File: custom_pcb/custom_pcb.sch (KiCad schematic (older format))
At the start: 205 parts, among them J1 USB_mini_micro_B, K0 KEYSW, K1 KEYSW, K10 KEYSW, K11 KEYSW, K12 KEYSW, K13 KEYSW, K14 KEYSW, K15 KEYSW, K16 KEYSW, K17 KEYSW, K18 KEYSW, K19 KEYSW, K2 KEYSW, K20 KEYSW, K21 KEYSW, K22 KEYSW, K23 KEYSW, K24 KEYSW, K25 KEYSW, K26 KEYSW, K27 KEYSW, K28 KEYSW, K29 KEYSW, K3 KEYSW, K30 KEYSW, K31 KEYSW, K32 KEYSW, K33 KEYSW, K34 KEYSW, K35 KEYSW, K36 KEYSW, K37 KEYSW, K38 KEYSW, K39 KEYSW, K4 KEYSW, K40 KEYSW, K41 KEYSW, K42 KEYSW, K43 KEYSW, K44 KEYSW, K45 KEYSW, K46 KEYSW, K47 KEYSW, K48 KEYSW, K49 KEYSW, K5 KEYSW, K50 KEYSW, K51 KEYSW, K52 KEYSW, K53 KEYSW, K54 KEYSW, K55 KEYSW, K56 KEYSW, K57 KEYSW, K58 KEYSW, K59 KEYSW, K6 KEYSW, K60 KEYSW, K61 KEYSW, K62 KEYSW, K63 KEYSW, K64 KEYSW, K65 KEYSW, K66 KEYSW, K67 KEYSW, K68 KEYSW, K69 KEYSW, K7 KEYSW, K70 KEYSW, K71 KEYSW, K72 KEYSW, K73 KEYSW, K74 KEYSW, K75 KEYSW, K76 KEYSW, K77 KEYSW, K78 KEYSW, K79 KEYSW, K8 KEYSW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

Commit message: cpcb more routing
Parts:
- removed D89, D90, D91, D92, D93, D94, D95, D96, D97, D98, D99: D, Diodes_SMD:D_SOD-123, symbol D
- removed K92, K93, K94, K95, K96, K97, K98, K99: KEYSW, cherry_rgb:CHERRY_PLATE_NH_100H, symbol KEYSW
- renumbered K90 to MOUSE0, K91 to MOUSE1, K89 to MOUSE2
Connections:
- net labels removed: col9
- wire segments 112 -> 108
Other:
- moved on the sheet: MOUSE0, MOUSE1, MOUSE2

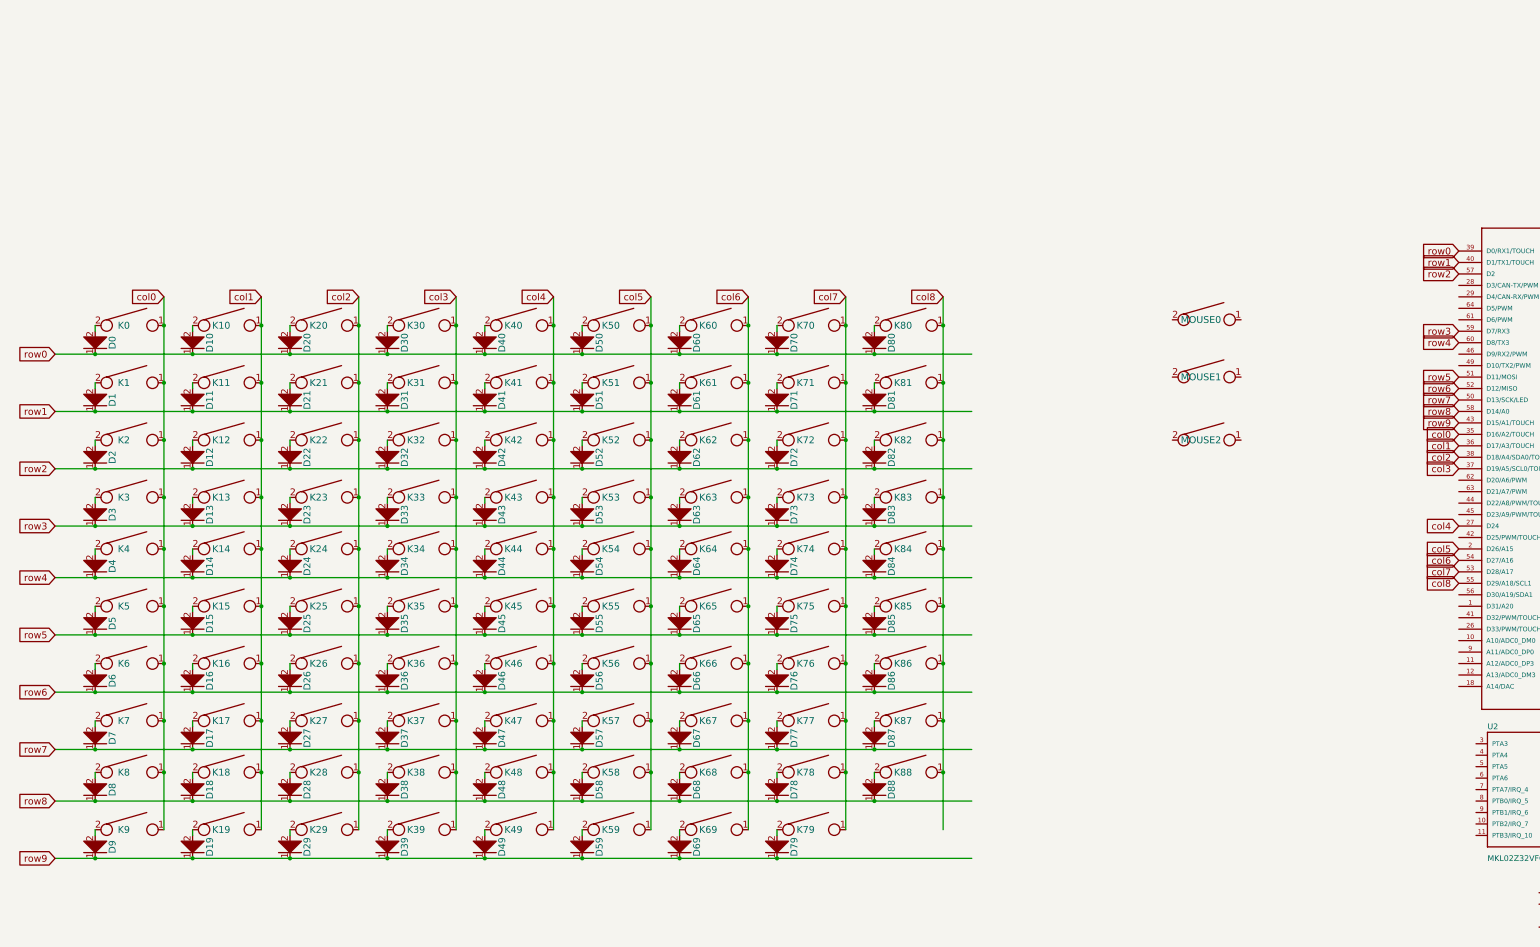
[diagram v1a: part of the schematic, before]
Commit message: cpcb switched to 7x14 matrix finished first pass routing
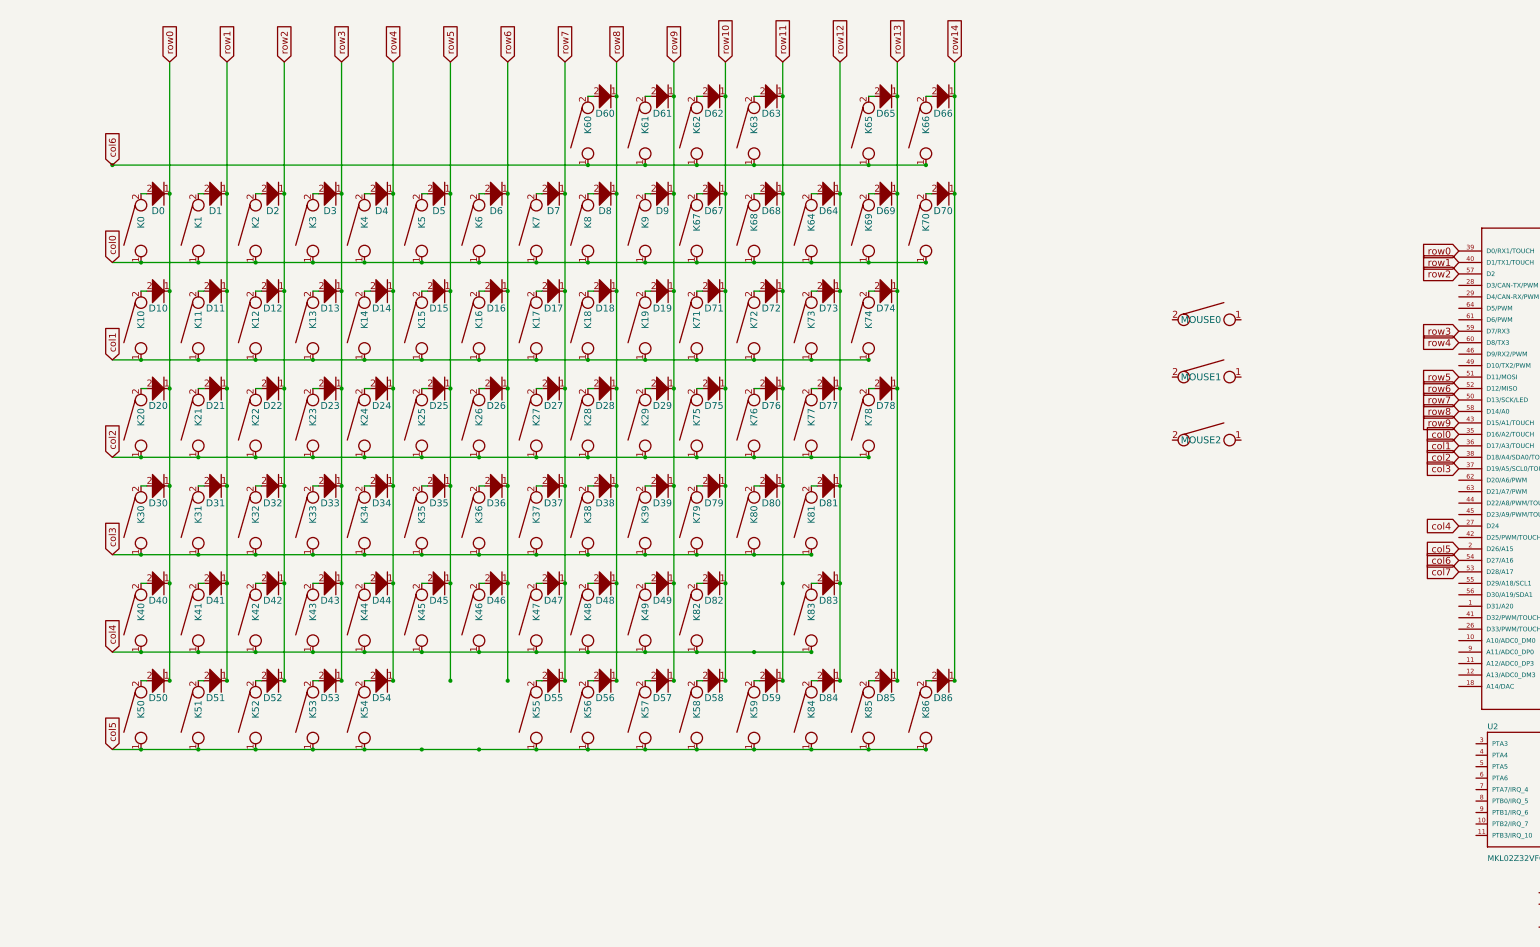
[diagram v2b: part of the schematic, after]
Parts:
- removed D87, D88: D, Diodes_SMD:D_SOD-123, symbol D
- removed K87, K88: KEYSW, cherry_rgb:CHERRY_PLATE_NH_100H, symbol KEYSW
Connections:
- net labels added: row10, row11, row12, row13, row14
- net labels removed: col8
- wire segments 108 -> 109
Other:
- moved on the sheet: D0, D1, D10, D11, D12, D13, D14, D15, D16, D17, D18, D19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

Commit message: cpcb routing of rows and columns complete
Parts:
- added P1: CONN_01X08, Connectors_Molex:Molex_PicoBlade_53261-0871_08x1.25mm_Angled, symbol CONN_01X08
- added U4, U5, U6: STP16CP05, Housings_SSOP:TSSOP-24_4.4x7.8mm_Pitch0.65mm, symbol STP16CP05
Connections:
- net col0: now also U1.59 (D7/RX3); no longer U1.35 (D16/A2/TOUCH)
- net col1: now also U1.60 (D8/TX3); no longer U1.36 (D17/A3/TOUCH)
- net col2: now also U1.61 (D6/PWM); no longer U1.38 (D18/A4/SDA0/TOUCH)
- net col3: now also U1.62 (D20/A6/PWM); no longer U1.37 (D19/A5/SCL0/TOUCH)
- net col4: now also U1.63 (D21/A7/PWM); no longer U1.27 (D24)
- net col5: now also U1.64 (D5/PWM); no longer U1.2 (D26/A15)
- net col6: now also U1.35 (D16/A2/TOUCH); no longer U1.54 (D27/A16)
- net row0: now also U1.58 (D14/A0); no longer U1.39 (D0/RX1/TOUCH)
- net row1: now also U1.57 (D2); no longer U1.40 (D1/TX1/TOUCH)
- net row10: now also U1.40 (D1/TX1/TOUCH)
- net row11: now also U1.39 (D0/RX1/TOUCH)
- net row12: now also U1.38 (D18/A4/SDA0/TOUCH)
- net row13: now also U1.37 (D19/A5/SCL0/TOUCH)
- net row14: now also U1.36 (D17/A3/TOUCH)
- net row2: now also U1.56 (D30/A19/SDA1); no longer U1.57 (D2)
- net row3: now also U1.55 (D29/A18/SCL1); no longer U1.59 (D7/RX3)
- net row4: now also U1.46 (D9/RX2/PWM); no longer U1.60 (D8/TX3)
- net row5: now also U1.45 (D23/A9/PWM/TOUCH); no longer U1.51 (D11/MOSI)
- net row6: now also U1.44 (D22/A8/PWM/TOUCH); no longer U1.52 (D12/MISO)
- net row7: now also U1.43 (D15/A1/TOUCH); no longer U1.50 (D13/SCK/LED)
- net row8: now also U1.42 (D25/PWM/TOUCH); no longer U1.58 (D14/A0)
- net row9: now also U1.41 (D32/PWM/TOUCH); no longer U1.43 (D15/A1/TOUCH)
- net TP_DATA: now reaches U1.1 (D31/A20)
- net TP_DATA: now also P1.2 (P2)
- net GND: now reaches U1.15 (VREF-L)
- net GND: now also P1.1 (P1)
- net LED_DATA1: now reaches U1.28 (D3/CAN-TX/PWM)
- net LED_DATA2: now reaches U1.29 (D4/CAN-RX/PWM)
- net LED_CLK: now reaches U1.49 (D10/TX2/PWM)
- net BTN0: now reaches MOUSE0.1
- net BTN0: now also P1.6 (P6)
- net BTN1: now reaches MOUSE1.1
- net BTN1: now also P1.7 (P7)
- net BTN2: now reaches MOUSE2.1
- net BTN2: now also P1.8 (P8)
- net col7: no longer names the net of U1.53 (D28/A17)
- new net LED_DATA0: U1.27 (D24)
- new net TP_5V: P1.5 (P5)
- new net TP_CLK: P1.3 (P3), U1.2 (D26/A15)
- new net TP_RST: P1.4 (P4)
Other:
- note added: "Note that when wiring the LVC9 -> mainboard \nconnector the BTN0 and BTN2 leads need to be\nswapped since the order is reversed here to simplify routing."
- moved on the sheet: D0, D1, D10, D11, D12, D13, D14, D15, D16, D17, D18, D19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

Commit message: wiring cleanup
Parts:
- removed X1: XTAL, symbol XTAL
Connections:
- net GND: now also MOUSE0.2, MOUSE1.2, MOUSE2.2
- net LED_CLK: now also U4.3 (CLK), U5.3 (CLK), U6.3 (CLK)
- net LED_DATA0: now also U4.2 (SDI)
- net LED_DATA1: now also U5.2 (SDI)
- net LED_DATA2: now also U6.2 (SDI)
- net row0: no longer D0.1, D10.1, D20.1, D30.1, D40.1, D50.1
- net row1: no longer D1.1, D11.1, D21.1, D31.1, D41.1, D51.1
- net row10: no longer D58.1, D62.1, D67.1, D71.1, D75.1, D79.1, D82.1
- net row11: no longer D59.1, D63.1, D68.1, D72.1, D76.1, D80.1
- net row12: no longer D64.1, D73.1, D77.1, D81.1, D83.1, D84.1
- net row13: no longer D65.1, D69.1, D74.1, D78.1, D85.1
- net row14: no longer D66.1, D70.1, D86.1
- net row2: no longer D12.1, D2.1, D22.1, D32.1, D42.1, D52.1
- net row3: no longer D13.1, D23.1, D3.1, D33.1, D43.1, D53.1
- net row4: no longer D14.1, D24.1, D34.1, D4.1, D44.1, D54.1
- net row5: no longer D15.1, D25.1, D35.1, D45.1, D5.1
- net row6: no longer D16.1, D26.1, D36.1, D46.1, D6.1
- net row7: no longer D17.1, D27.1, D37.1, D47.1, D55.1, D7.1
- net row8: no longer D18.1, D28.1, D38.1, D48.1, D56.1, D60.1, D8.1
- net row9: no longer D19.1, D29.1, D39.1, D49.1, D57.1, D61.1, D9.1
- new net c0: D0.1, D10.1, D20.1, D30.1, D40.1, D50.1
- new net c1: D1.1, D11.1, D21.1, D31.1, D41.1, D51.1
- new net c10: D58.1, D62.1, D67.1, D71.1, D75.1, D79.1, D82.1
- new net c11: D59.1, D63.1, D68.1, D72.1, D76.1, D80.1
- new net c12: D64.1, D73.1, D77.1, D81.1, D83.1, D84.1
- new net c13: D65.1, D69.1, D74.1, D78.1, D85.1
- new net c14: D66.1, D70.1, D86.1
- new net c2: D12.1, D2.1, D22.1, D32.1, D42.1, D52.1
- new net c3: D13.1, D23.1, D3.1, D33.1, D43.1, D53.1
- new net c4: D14.1, D24.1, D34.1, D4.1, D44.1, D54.1
- new net c5: D15.1, D25.1, D35.1, D45.1, D5.1
- new net c6: D16.1, D26.1, D36.1, D46.1, D6.1
- new net c7: D17.1, D27.1, D37.1, D47.1, D55.1, D7.1
- new net c8: D18.1, D28.1, D38.1, D48.1, D56.1, D60.1, D8.1
- new net c9: D19.1, D29.1, D39.1, D49.1, D57.1, D61.1, D9.1

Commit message: cpcb started led work
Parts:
- added R0, R1, R2, R3, R4, R5, R6: R, symbol R
- added SMD_LED0, SMD_LED1, SMD_LED10, SMD_LED100, SMD_LED101, SMD_LED102, SMD_LED103, SMD_LED104, SMD_LED11, SMD_LED12, SMD_LED13, SMD_LED14, SMD_LED15, SMD_LED16, SMD_LED17, SMD_LED18, SMD_LED19, SMD_LED2, SMD_LED20, SMD_LED21, SMD_LED22, SMD_LED23, SMD_LED24, SMD_LED25, SMD_LED26, SMD_LED27, SMD_LED28, SMD_LED29, SMD_LED3, SMD_LED30, SMD_LED31, SMD_LED32, SMD_LED33, SMD_LED34, SMD_LED35, SMD_LED36, SMD_LED37, SMD_LED38, SMD_LED39, SMD_LED4, SMD_LED40, SMD_LED41, SMD_LED42, SMD_LED43, SMD_LED44, SMD_LED45, SMD_LED46, SMD_LED47, SMD_LED48, SMD_LED49, SMD_LED5, SMD_LED50, SMD_LED51, SMD_LED52, SMD_LED53, SMD_LED54, SMD_LED55, SMD_LED56, SMD_LED57, SMD_LED58, SMD_LED59, SMD_LED6, SMD_LED60, SMD_LED61, SMD_LED62, SMD_LED63, SMD_LED64, SMD_LED65, SMD_LED66, SMD_LED67, SMD_LED68, SMD_LED69, SMD_LED7, SMD_LED70, SMD_LED71, SMD_LED72, SMD_LED73, SMD_LED74, SMD_LED75, SMD_LED76, SMD_LED77, SMD_LED78, SMD_LED79, SMD_LED8, SMD_LED80, SMD_LED81, SMD_LED82, SMD_LED83, SMD_LED84, SMD_LED85, SMD_LED86, SMD_LED87, SMD_LED88, SMD_LED89, SMD_LED9, SMD_LED90, SMD_LED91, SMD_LED92, SMD_LED93, SMD_LED94, SMD_LED95, SMD_LED96, SMD_LED97, SMD_LED98, SMD_LED99: SMLVN6RGB, symbol SMLVN6RGB
- K0, K64: footprint cherry_rgb:CHERRY_PLATE_NH_100H -> cherry_rgb:CHERRY_PLATE_150V
- K20, K56, K78: footprint cherry_rgb:CHERRY_PLATE_NH_100H -> cherry_rgb:CHERRY_PLATE_150H
- K30, MOUSE0, MOUSE2: footprint cherry_rgb:CHERRY_PLATE_NH_100H -> cherry_rgb:CHERRY_PLATE_175H
- K40, K81: footprint cherry_rgb:CHERRY_PLATE_NH_100H -> cherry_rgb:CHERRY_PLATE_225H
- K51, K55: footprint cherry_rgb:CHERRY_PLATE_NH_100H -> cherry_rgb:CHERRY_PLATE_125H
- K54: footprint cherry_rgb:CHERRY_PLATE_NH_100H -> cherry_rgb:CHERRY_PLATE_NH_5000H
- K74: footprint cherry_rgb:CHERRY_PLATE_NH_100H -> cherry_rgb:CHERRY_PLATE_200H
- K83: footprint cherry_rgb:CHERRY_PLATE_NH_100H -> cherry_rgb:CHERRY_PLATE_275H
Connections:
- net row0 is gone; now on net c0: U1.58 (D14/A0)
- net row1 is gone; now on net c1: U1.57 (D2)
- net row10 is gone; now on net c10: U1.40 (D1/TX1/TOUCH)
- net row11 is gone; now on net c11: U1.39 (D0/RX1/TOUCH)
- net row12 is gone; now on net c12: U1.38 (D18/A4/SDA0/TOUCH)
- net row13 is gone; now on net c13: U1.37 (D19/A5/SCL0/TOUCH)
- net row14 is gone; now on net c14: U1.36 (D17/A3/TOUCH)
- net row2 is gone; now on net c2: U1.56 (D30/A19/SDA1)
- net row3 is gone; now on net c3: U1.55 (D29/A18/SCL1)
- net row4 is gone; now on net c4: U1.46 (D9/RX2/PWM)
- net row5 is gone; now on net c5: U1.45 (D23/A9/PWM/TOUCH)
- net row6 is gone; now on net c6: U1.44 (D22/A8/PWM/TOUCH)
- net row7 is gone; now on net c7: U1.43 (D15/A1/TOUCH)
- net row8 is gone; now on net c8: U1.42 (D25/PWM/TOUCH)
- net row9 is gone; now on net c9: U1.41 (D32/PWM/TOUCH)
- net anode5: now reaches U4.10 (OUT5)
- net anode5: now also SMD_LED20.1 (RK), SMD_LED20.2 (GK), SMD_LED20.3 (BK), SMD_LED35.1 (RK), SMD_LED35.2 (GK), SMD_LED35.3 (BK), SMD_LED5.1 (RK), SMD_LED5.2 (GK), SMD_LED5.3 (BK), SMD_LED50.1 (RK), SMD_LED50.2 (GK), SMD_LED50.3 (BK), SMD_LED65.1 (RK), SMD_LED65.2 (GK), SMD_LED65.3 (BK), SMD_LED80.1 (RK), SMD_LED80.2 (GK), SMD_LED80.3 (BK), SMD_LED95.1 (RK), SMD_LED95.2 (GK), SMD_LED95.3 (BK)
- net anode6: now reaches U4.11 (OUT6)
- net anode6: now also SMD_LED21.1 (RK), SMD_LED21.2 (GK), SMD_LED21.3 (BK), SMD_LED36.1 (RK), SMD_LED36.2 (GK), SMD_LED36.3 (BK), SMD_LED51.1 (RK), SMD_LED51.2 (GK), SMD_LED51.3 (BK), SMD_LED6.1 (RK), SMD_LED6.2 (GK), SMD_LED6.3 (BK), SMD_LED66.1 (RK), SMD_LED66.2 (GK), SMD_LED66.3 (BK), SMD_LED81.1 (RK), SMD_LED81.2 (GK), SMD_LED81.3 (BK), SMD_LED96.1 (RK), SMD_LED96.2 (GK), SMD_LED96.3 (BK)
- net anode7: now reaches U4.12 (OUT7)
- net anode7: now also SMD_LED22.1 (RK), SMD_LED22.2 (GK), SMD_LED22.3 (BK), SMD_LED37.1 (RK), SMD_LED37.2 (GK), SMD_LED37.3 (BK), SMD_LED52.1 (RK), SMD_LED52.2 (GK), SMD_LED52.3 (BK), SMD_LED67.1 (RK), SMD_LED67.2 (GK), SMD_LED67.3 (BK), SMD_LED7.1 (RK), SMD_LED7.2 (GK), SMD_LED7.3 (BK), SMD_LED82.1 (RK), SMD_LED82.2 (GK), SMD_LED82.3 (BK), SMD_LED97.1 (RK), SMD_LED97.2 (GK), SMD_LED97.3 (BK)
- net anode8: now reaches U4.13 (OUT8)
- net anode8: now also SMD_LED23.1 (RK), SMD_LED23.2 (GK), SMD_LED23.3 (BK), SMD_LED38.1 (RK), SMD_LED38.2 (GK), SMD_LED38.3 (BK), SMD_LED53.1 (RK), SMD_LED53.2 (GK), SMD_LED53.3 (BK), SMD_LED68.1 (RK), SMD_LED68.2 (GK), SMD_LED68.3 (BK), SMD_LED8.1 (RK), SMD_LED8.2 (GK), SMD_LED8.3 (BK), SMD_LED83.1 (RK), SMD_LED83.2 (GK), SMD_LED83.3 (BK), SMD_LED98.1 (RK), SMD_LED98.2 (GK), SMD_LED98.3 (BK)
- net anode9: now reaches U4.14 (OUT9)
- net anode9: now also SMD_LED24.1 (RK), SMD_LED24.2 (GK), SMD_LED24.3 (BK), SMD_LED39.1 (RK), SMD_LED39.2 (GK), SMD_LED39.3 (BK), SMD_LED54.1 (RK), SMD_LED54.2 (GK), SMD_LED54.3 (BK), SMD_LED69.1 (RK), SMD_LED69.2 (GK), SMD_LED69.3 (BK), SMD_LED84.1 (RK), SMD_LED84.2 (GK), SMD_LED84.3 (BK), SMD_LED9.1 (RK), SMD_LED9.2 (GK), SMD_LED9.3 (BK), SMD_LED99.1 (RK), SMD_LED99.2 (GK), SMD_LED99.3 (BK)
- net anode10: now reaches U4.15 (OUT10)
- net anode10: now also SMD_LED10.1 (RK), SMD_LED10.2 (GK), SMD_LED10.3 (BK), SMD_LED100.1 (RK), SMD_LED100.2 (GK), SMD_LED100.3 (BK), SMD_LED25.1 (RK), SMD_LED25.2 (GK), SMD_LED25.3 (BK), SMD_LED40.1 (RK), SMD_LED40.2 (GK), SMD_LED40.3 (BK), SMD_LED55.1 (RK), SMD_LED55.2 (GK), SMD_LED55.3 (BK), SMD_LED70.1 (RK), SMD_LED70.2 (GK), SMD_LED70.3 (BK), SMD_LED85.1 (RK), SMD_LED85.2 (GK), SMD_LED85.3 (BK)
- net anode11: now reaches U4.16 (OUT11)
- net anode11: now also SMD_LED101.1 (RK), SMD_LED101.2 (GK), SMD_LED101.3 (BK), SMD_LED11.1 (RK), SMD_LED11.2 (GK), SMD_LED11.3 (BK), SMD_LED26.1 (RK), SMD_LED26.2 (GK), SMD_LED26.3 (BK), SMD_LED41.1 (RK), SMD_LED41.2 (GK), SMD_LED41.3 (BK), SMD_LED56.1 (RK), SMD_LED56.2 (GK), SMD_LED56.3 (BK), SMD_LED71.1 (RK), SMD_LED71.2 (GK), SMD_LED71.3 (BK), SMD_LED86.1 (RK), SMD_LED86.2 (GK), SMD_LED86.3 (BK)
- net anode12: now reaches U4.17 (OUT12)
- net anode12: now also SMD_LED102.1 (RK), SMD_LED102.2 (GK), SMD_LED102.3 (BK), SMD_LED12.1 (RK), SMD_LED12.2 (GK), SMD_LED12.3 (BK), SMD_LED27.1 (RK), SMD_LED27.2 (GK), SMD_LED27.3 (BK), SMD_LED42.1 (RK), SMD_LED42.2 (GK), SMD_LED42.3 (BK), SMD_LED57.1 (RK), SMD_LED57.2 (GK), SMD_LED57.3 (BK), SMD_LED72.1 (RK), SMD_LED72.2 (GK), SMD_LED72.3 (BK), SMD_LED87.1 (RK), SMD_LED87.2 (GK), SMD_LED87.3 (BK)
- net anode13: now reaches U4.18 (OUT13)
- net anode13: now also SMD_LED103.1 (RK), SMD_LED103.2 (GK), SMD_LED103.3 (BK), SMD_LED13.1 (RK), SMD_LED13.2 (GK), SMD_LED13.3 (BK), SMD_LED28.1 (RK), SMD_LED28.2 (GK), SMD_LED28.3 (BK), SMD_LED43.1 (RK), SMD_LED43.2 (GK), SMD_LED43.3 (BK), SMD_LED58.1 (RK), SMD_LED58.2 (GK), SMD_LED58.3 (BK), SMD_LED73.1 (RK), SMD_LED73.2 (GK), SMD_LED73.3 (BK), SMD_LED88.1 (RK), SMD_LED88.2 (GK), SMD_LED88.3 (BK)
- net anode14: now reaches U4.19 (OUT14)
- net anode14: now also SMD_LED104.1 (RK), SMD_LED104.2 (GK), SMD_LED104.3 (BK), SMD_LED14.1 (RK), SMD_LED14.2 (GK), SMD_LED14.3 (BK), SMD_LED29.1 (RK), SMD_LED29.2 (GK), SMD_LED29.3 (BK), SMD_LED44.1 (RK), SMD_LED44.2 (GK), SMD_LED44.3 (BK), SMD_LED59.1 (RK), SMD_LED59.2 (GK), SMD_LED59.3 (BK), SMD_LED74.1 (RK), SMD_LED74.2 (GK), SMD_LED74.3 (BK), SMD_LED89.1 (RK), SMD_LED89.2 (GK), SMD_LED89.3 (BK)
- net anode0: now reaches U4.5 (OUT0)
- net anode0: now also SMD_LED0.1 (RK), SMD_LED0.2 (GK), SMD_LED0.3 (BK), SMD_LED15.1 (RK), SMD_LED15.2 (GK), SMD_LED15.3 (BK), SMD_LED30.1 (RK), SMD_LED30.2 (GK), SMD_LED30.3 (BK), SMD_LED45.1 (RK), SMD_LED45.2 (GK), SMD_LED45.3 (BK), SMD_LED60.1 (RK), SMD_LED60.2 (GK), SMD_LED60.3 (BK), SMD_LED75.1 (RK), SMD_LED75.2 (GK), SMD_LED75.3 (BK), SMD_LED90.1 (RK), SMD_LED90.2 (GK), SMD_LED90.3 (BK)
- net anode1: now reaches U4.6 (OUT1)
- net anode1: now also SMD_LED1.1 (RK), SMD_LED1.2 (GK), SMD_LED1.3 (BK), SMD_LED16.1 (RK), SMD_LED16.2 (GK), SMD_LED16.3 (BK), SMD_LED31.1 (RK), SMD_LED31.2 (GK), SMD_LED31.3 (BK), SMD_LED46.1 (RK), SMD_LED46.2 (GK), SMD_LED46.3 (BK), SMD_LED61.1 (RK), SMD_LED61.2 (GK), SMD_LED61.3 (BK), SMD_LED76.1 (RK), SMD_LED76.2 (GK), SMD_LED76.3 (BK), SMD_LED91.1 (RK), SMD_LED91.2 (GK), SMD_LED91.3 (BK)
- net anode2: now reaches U4.7 (OUT2)
- net anode2: now also SMD_LED17.1 (RK), SMD_LED17.2 (GK), SMD_LED17.3 (BK), SMD_LED2.1 (RK), SMD_LED2.2 (GK), SMD_LED2.3 (BK), SMD_LED32.1 (RK), SMD_LED32.2 (GK), SMD_LED32.3 (BK), SMD_LED47.1 (RK), SMD_LED47.2 (GK), SMD_LED47.3 (BK), SMD_LED62.1 (RK), SMD_LED62.2 (GK), SMD_LED62.3 (BK), SMD_LED77.1 (RK), SMD_LED77.2 (GK), SMD_LED77.3 (BK), SMD_LED92.1 (RK), SMD_LED92.2 (GK), SMD_LED92.3 (BK)
- net anode3: now reaches U4.8 (OUT3)
- net anode3: now also SMD_LED18.1 (RK), SMD_LED18.2 (GK), SMD_LED18.3 (BK), SMD_LED3.1 (RK), SMD_LED3.2 (GK), SMD_LED3.3 (BK), SMD_LED33.1 (RK), SMD_LED33.2 (GK), SMD_LED33.3 (BK), SMD_LED48.1 (RK), SMD_LED48.2 (GK), SMD_LED48.3 (BK), SMD_LED63.1 (RK), SMD_LED63.2 (GK), SMD_LED63.3 (BK), SMD_LED78.1 (RK), SMD_LED78.2 (GK), SMD_LED78.3 (BK), SMD_LED93.1 (RK), SMD_LED93.2 (GK), SMD_LED93.3 (BK)
- net anode4: now reaches U4.9 (OUT4)
- net anode4: now also SMD_LED19.1 (RK), SMD_LED19.2 (GK), SMD_LED19.3 (BK), SMD_LED34.1 (RK), SMD_LED34.2 (GK), SMD_LED34.3 (BK), SMD_LED4.1 (RK), SMD_LED4.2 (GK), SMD_LED4.3 (BK), SMD_LED49.1 (RK), SMD_LED49.2 (GK), SMD_LED49.3 (BK), SMD_LED64.1 (RK), SMD_LED64.2 (GK), SMD_LED64.3 (BK), SMD_LED79.1 (RK), SMD_LED79.2 (GK), SMD_LED79.3 (BK), SMD_LED94.1 (RK), SMD_LED94.2 (GK), SMD_LED94.3 (BK)
- net col0 renamed r0
- net col1 renamed r1
- net col2 renamed r2
- net col3 renamed r3
- net col4 renamed r4
- net col5 renamed r5
- net col6 renamed r6
- new net: R6.1, SMD_LED100.5 (GA), SMD_LED101.5 (GA), SMD_LED102.5 (GA), SMD_LED103.5 (GA), SMD_LED104.5 (GA), SMD_LED90.5 (GA), SMD_LED91.5 (GA), SMD_LED92.5 (GA), SMD_LED93.5 (GA), SMD_LED94.5 (GA), SMD_LED95.5 (GA), SMD_LED96.5 (GA), SMD_LED97.5 (GA), SMD_LED98.5 (GA), SMD_LED99.5 (GA)
- new net: R5.1, SMD_LED75.5 (GA), SMD_LED76.5 (GA), SMD_LED77.5 (GA), SMD_LED78.5 (GA), SMD_LED79.5 (GA), SMD_LED80.5 (GA), SMD_LED81.5 (GA), SMD_LED82.5 (GA), SMD_LED83.5 (GA), SMD_LED84.5 (GA), SMD_LED85.5 (GA), SMD_LED86.5 (GA), SMD_LED87.5 (GA), SMD_LED88.5 (GA), SMD_LED89.5 (GA)
- new net: R4.1, SMD_LED60.5 (GA), SMD_LED61.5 (GA), SMD_LED62.5 (GA), SMD_LED63.5 (GA), SMD_LED64.5 (GA), SMD_LED65.5 (GA), SMD_LED66.5 (GA), SMD_LED67.5 (GA), SMD_LED68.5 (GA), SMD_LED69.5 (GA), SMD_LED70.5 (GA), SMD_LED71.5 (GA), SMD_LED72.5 (GA), SMD_LED73.5 (GA), SMD_LED74.5 (GA)
- new net: R3.1, SMD_LED45.5 (GA), SMD_LED46.5 (GA), SMD_LED47.5 (GA), SMD_LED48.5 (GA), SMD_LED49.5 (GA), SMD_LED50.5 (GA), SMD_LED51.5 (GA), SMD_LED52.5 (GA), SMD_LED53.5 (GA), SMD_LED54.5 (GA), SMD_LED55.5 (GA), SMD_LED56.5 (GA), SMD_LED57.5 (GA), SMD_LED58.5 (GA), SMD_LED59.5 (GA)
- new net: R2.1, SMD_LED30.5 (GA), SMD_LED31.5 (GA), SMD_LED32.5 (GA), SMD_LED33.5 (GA), SMD_LED34.5 (GA), SMD_LED35.5 (GA), SMD_LED36.5 (GA), SMD_LED37.5 (GA), SMD_LED38.5 (GA), SMD_LED39.5 (GA), SMD_LED40.5 (GA), SMD_LED41.5 (GA), SMD_LED42.5 (GA), SMD_LED43.5 (GA), SMD_LED44.5 (GA)
- new net: R1.1, SMD_LED15.5 (GA), SMD_LED16.5 (GA), SMD_LED17.5 (GA), SMD_LED18.5 (GA), SMD_LED19.5 (GA), SMD_LED20.5 (GA), SMD_LED21.5 (GA), SMD_LED22.5 (GA), SMD_LED23.5 (GA), SMD_LED24.5 (GA), SMD_LED25.5 (GA), SMD_LED26.5 (GA), SMD_LED27.5 (GA), SMD_LED28.5 (GA), SMD_LED29.5 (GA)
- new net: R0.1, SMD_LED0.5 (GA), SMD_LED1.5 (GA), SMD_LED10.5 (GA), SMD_LED11.5 (GA), SMD_LED12.5 (GA), SMD_LED13.5 (GA), SMD_LED14.5 (GA), SMD_LED2.5 (GA), SMD_LED3.5 (GA), SMD_LED4.5 (GA), SMD_LED5.5 (GA), SMD_LED6.5 (GA), SMD_LED7.5 (GA), SMD_LED8.5 (GA), SMD_LED9.5 (GA)
- new net blue0: SMD_LED0.6 (RA), SMD_LED1.6 (RA), SMD_LED10.6 (RA), SMD_LED11.6 (RA), SMD_LED12.6 (RA), SMD_LED13.6 (RA), SMD_LED14.6 (RA), SMD_LED2.6 (RA), SMD_LED3.6 (RA), SMD_LED4.6 (RA), SMD_LED5.6 (RA), SMD_LED6.6 (RA), SMD_LED7.6 (RA), SMD_LED8.6 (RA), SMD_LED9.6 (RA)
- new net blue1: SMD_LED15.6 (RA), SMD_LED16.6 (RA), SMD_LED17.6 (RA), SMD_LED18.6 (RA), SMD_LED19.6 (RA), SMD_LED20.6 (RA), SMD_LED21.6 (RA), SMD_LED22.6 (RA), SMD_LED23.6 (RA), SMD_LED24.6 (RA), SMD_LED25.6 (RA), SMD_LED26.6 (RA), SMD_LED27.6 (RA), SMD_LED28.6 (RA), SMD_LED29.6 (RA)
- new net blue2: SMD_LED30.6 (RA), SMD_LED31.6 (RA), SMD_LED32.6 (RA), SMD_LED33.6 (RA), SMD_LED34.6 (RA), SMD_LED35.6 (RA), SMD_LED36.6 (RA), SMD_LED37.6 (RA), SMD_LED38.6 (RA), SMD_LED39.6 (RA), SMD_LED40.6 (RA), SMD_LED41.6 (RA), SMD_LED42.6 (RA), SMD_LED43.6 (RA), SMD_LED44.6 (RA)
- new net blue3: SMD_LED45.6 (RA), SMD_LED46.6 (RA), SMD_LED47.6 (RA), SMD_LED48.6 (RA), SMD_LED49.6 (RA), SMD_LED50.6 (RA), SMD_LED51.6 (RA), SMD_LED52.6 (RA), SMD_LED53.6 (RA), SMD_LED54.6 (RA), SMD_LED55.6 (RA), SMD_LED56.6 (RA), SMD_LED57.6 (RA), SMD_LED58.6 (RA), SMD_LED59.6 (RA)
- new net blue4: SMD_LED60.6 (RA), SMD_LED61.6 (RA), SMD_LED62.6 (RA), SMD_LED63.6 (RA), SMD_LED64.6 (RA), SMD_LED65.6 (RA), SMD_LED66.6 (RA), SMD_LED67.6 (RA), SMD_LED68.6 (RA), SMD_LED69.6 (RA), SMD_LED70.6 (RA), SMD_LED71.6 (RA), SMD_LED72.6 (RA), SMD_LED73.6 (RA), SMD_LED74.6 (RA)
- new net blue5: SMD_LED75.6 (RA), SMD_LED76.6 (RA), SMD_LED77.6 (RA), SMD_LED78.6 (RA), SMD_LED79.6 (RA), SMD_LED80.6 (RA), SMD_LED81.6 (RA), SMD_LED82.6 (RA), SMD_LED83.6 (RA), SMD_LED84.6 (RA), SMD_LED85.6 (RA), SMD_LED86.6 (RA), SMD_LED87.6 (RA), SMD_LED88.6 (RA), SMD_LED89.6 (RA)
- new net blue6: SMD_LED100.6 (RA), SMD_LED101.6 (RA), SMD_LED102.6 (RA), SMD_LED103.6 (RA), SMD_LED104.6 (RA), SMD_LED90.6 (RA), SMD_LED91.6 (RA), SMD_LED92.6 (RA), SMD_LED93.6 (RA), SMD_LED94.6 (RA), SMD_LED95.6 (RA), SMD_LED96.6 (RA), SMD_LED97.6 (RA), SMD_LED98.6 (RA), SMD_LED99.6 (RA)
- new net green0: SMD_LED0.4 (BA), SMD_LED1.4 (BA), SMD_LED10.4 (BA), SMD_LED11.4 (BA), SMD_LED12.4 (BA), SMD_LED13.4 (BA), SMD_LED14.4 (BA), SMD_LED2.4 (BA), SMD_LED3.4 (BA), SMD_LED4.4 (BA), SMD_LED5.4 (BA), SMD_LED6.4 (BA), SMD_LED7.4 (BA), SMD_LED8.4 (BA), SMD_LED9.4 (BA)
- new net green1: SMD_LED15.4 (BA), SMD_LED16.4 (BA), SMD_LED17.4 (BA), SMD_LED18.4 (BA), SMD_LED19.4 (BA), SMD_LED20.4 (BA), SMD_LED21.4 (BA), SMD_LED22.4 (BA), SMD_LED23.4 (BA), SMD_LED24.4 (BA), SMD_LED25.4 (BA), SMD_LED26.4 (BA), SMD_LED27.4 (BA), SMD_LED28.4 (BA), SMD_LED29.4 (BA)
- new net green2: SMD_LED30.4 (BA), SMD_LED31.4 (BA), SMD_LED32.4 (BA), SMD_LED33.4 (BA), SMD_LED34.4 (BA), SMD_LED35.4 (BA), SMD_LED36.4 (BA), SMD_LED37.4 (BA), SMD_LED38.4 (BA), SMD_LED39.4 (BA), SMD_LED40.4 (BA), SMD_LED41.4 (BA), SMD_LED42.4 (BA), SMD_LED43.4 (BA), SMD_LED44.4 (BA)
- new net green3: SMD_LED45.4 (BA), SMD_LED46.4 (BA), SMD_LED47.4 (BA), SMD_LED48.4 (BA), SMD_LED49.4 (BA), SMD_LED50.4 (BA), SMD_LED51.4 (BA), SMD_LED52.4 (BA), SMD_LED53.4 (BA), SMD_LED54.4 (BA), SMD_LED55.4 (BA), SMD_LED56.4 (BA), SMD_LED57.4 (BA), SMD_LED58.4 (BA), SMD_LED59.4 (BA)
- new net green4: SMD_LED60.4 (BA), SMD_LED61.4 (BA), SMD_LED62.4 (BA), SMD_LED63.4 (BA), SMD_LED64.4 (BA), SMD_LED65.4 (BA), SMD_LED66.4 (BA), SMD_LED67.4 (BA), SMD_LED68.4 (BA), SMD_LED69.4 (BA), SMD_LED70.4 (BA), SMD_LED71.4 (BA), SMD_LED72.4 (BA), SMD_LED73.4 (BA), SMD_LED74.4 (BA)
- new net green5: SMD_LED75.4 (BA), SMD_LED76.4 (BA), SMD_LED77.4 (BA), SMD_LED78.4 (BA), SMD_LED79.4 (BA), SMD_LED80.4 (BA), SMD_LED81.4 (BA), SMD_LED82.4 (BA), SMD_LED83.4 (BA), SMD_LED84.4 (BA), SMD_LED85.4 (BA), SMD_LED86.4 (BA), SMD_LED87.4 (BA), SMD_LED88.4 (BA), SMD_LED89.4 (BA)
- new net green6: SMD_LED100.4 (BA), SMD_LED101.4 (BA), SMD_LED102.4 (BA), SMD_LED103.4 (BA), SMD_LED104.4 (BA), SMD_LED90.4 (BA), SMD_LED91.4 (BA), SMD_LED92.4 (BA), SMD_LED93.4 (BA), SMD_LED94.4 (BA), SMD_LED95.4 (BA), SMD_LED96.4 (BA), SMD_LED97.4 (BA), SMD_LED98.4 (BA), SMD_LED99.4 (BA)
- new net red0: R0.2
- new net red1: R1.2
- new net red2: R2.2
- new net red3: R3.2
- new net red4: R4.2
- new net red5: R5.2
- new net red6: R6.2
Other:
- note added: "Wire LEDs using common anode."
- moved on the sheet: D0, D1, D10, D11, D12, D13, D14, D15, D16, D17, D18, D19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

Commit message: cpcb led layout
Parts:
- R0, R1, R2, R3, R4, R5, R6: footprint (none) -> Resistors_SMD:R_0402
- SMD_LED0, SMD_LED1, SMD_LED10, SMD_LED100, SMD_LED101, SMD_LED102, SMD_LED103, SMD_LED104, SMD_LED11, SMD_LED12, SMD_LED13, SMD_LED14, SMD_LED15, SMD_LED16, SMD_LED17, SMD_LED18, SMD_LED19, SMD_LED2, SMD_LED20, SMD_LED21, SMD_LED22, SMD_LED23, SMD_LED24, SMD_LED25, SMD_LED26, SMD_LED27, SMD_LED28, SMD_LED29, SMD_LED3, SMD_LED30, SMD_LED31, SMD_LED32, SMD_LED33, SMD_LED34, SMD_LED35, SMD_LED36, SMD_LED37, SMD_LED38, SMD_LED39, SMD_LED4, SMD_LED40, SMD_LED41, SMD_LED42, SMD_LED43, SMD_LED44, SMD_LED45, SMD_LED46, SMD_LED47, SMD_LED48, SMD_LED49, SMD_LED5, SMD_LED50, SMD_LED51, SMD_LED52, SMD_LED53, SMD_LED54, SMD_LED55, SMD_LED56, SMD_LED57, SMD_LED58, SMD_LED59, SMD_LED6, SMD_LED60, SMD_LED61, SMD_LED62, SMD_LED63, SMD_LED64, SMD_LED65, SMD_LED66, SMD_LED67, SMD_LED68, SMD_LED69, SMD_LED7, SMD_LED70, SMD_LED71, SMD_LED72, SMD_LED73, SMD_LED74, SMD_LED75, SMD_LED76, SMD_LED77, SMD_LED78, SMD_LED79, SMD_LED8, SMD_LED80, SMD_LED81, SMD_LED82, SMD_LED83, SMD_LED84, SMD_LED85, SMD_LED86, SMD_LED87, SMD_LED88, SMD_LED89, SMD_LED9, SMD_LED90, SMD_LED91, SMD_LED92, SMD_LED93, SMD_LED94, SMD_LED95, SMD_LED96, SMD_LED97, SMD_LED98, SMD_LED99: footprint (none) -> cherry_rgb:SMLVN6RGB
